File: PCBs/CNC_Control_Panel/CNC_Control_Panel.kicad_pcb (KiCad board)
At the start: 2 copper layers, 100 x 100 mm, 45 parts, among them J1 Conn_01x07_Male, P1 Conn_02x20_Odd_Even, X0 SW_Push, Y0 SW_Push

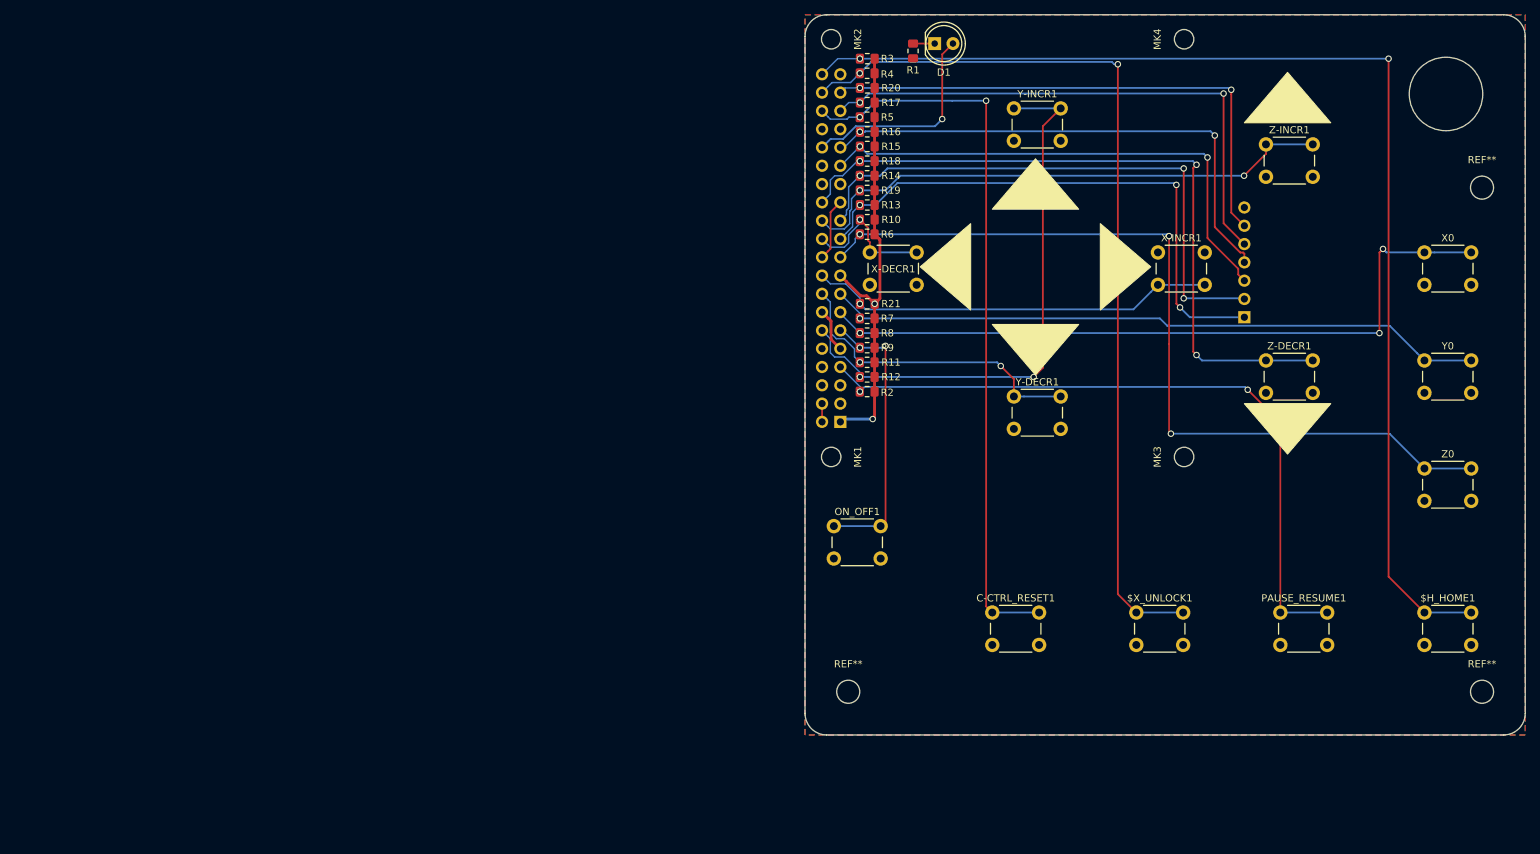
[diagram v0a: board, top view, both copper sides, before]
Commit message: reduced sheet size to A4
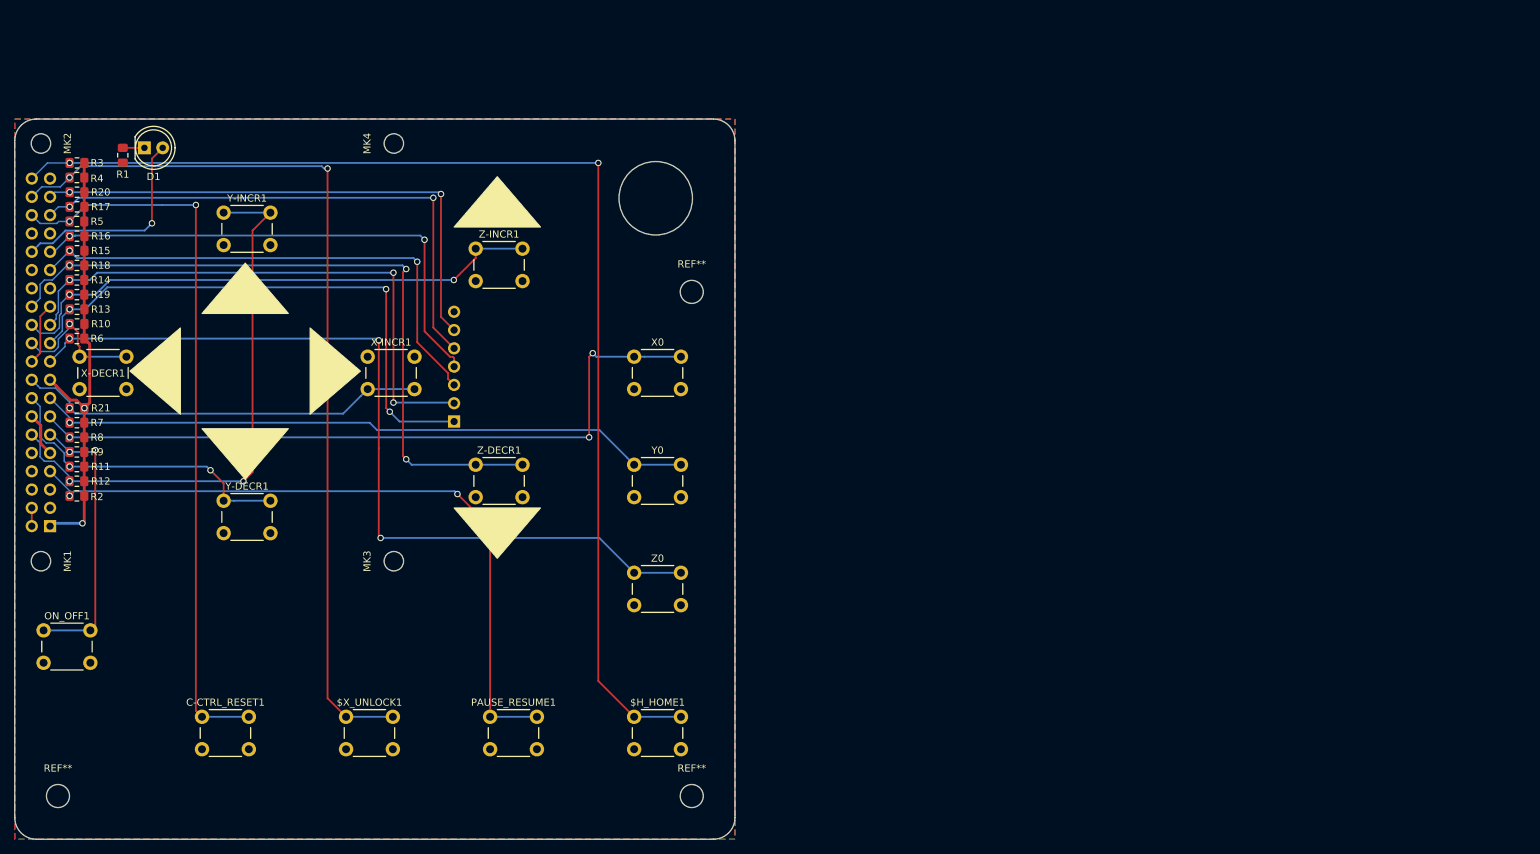
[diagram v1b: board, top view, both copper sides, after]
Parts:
- moved C-CTRL_RESET1 110.7 mm to (60.3, 160.5)
- moved D1 110.7 mm to (52.3, 81.5)
- moved ON_OFF1 110.7 mm to (38.3, 148.5)
- moved R1 110.7 mm to (49.3, 82.5)
- moved R10 110.7 mm to (42.9, 105.9)
- moved R11 110.7 mm to (42.9, 125.7)
- moved R12 110.7 mm to (42.9, 127.8)
- moved R13 110.7 mm to (42.9, 103.9)
- moved R14 110.7 mm to (42.9, 99.8)
- moved R15 110.7 mm to (42.9, 95.8)
- moved R16 110.7 mm to (42.9, 93.7)
- moved R17 110.7 mm to (42.9, 89.7)
- moved R19 110.7 mm to (42.9, 101.9)
- moved R2 110.7 mm to (42.9, 129.8)
- moved R20 110.7 mm to (42.9, 87.6)
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
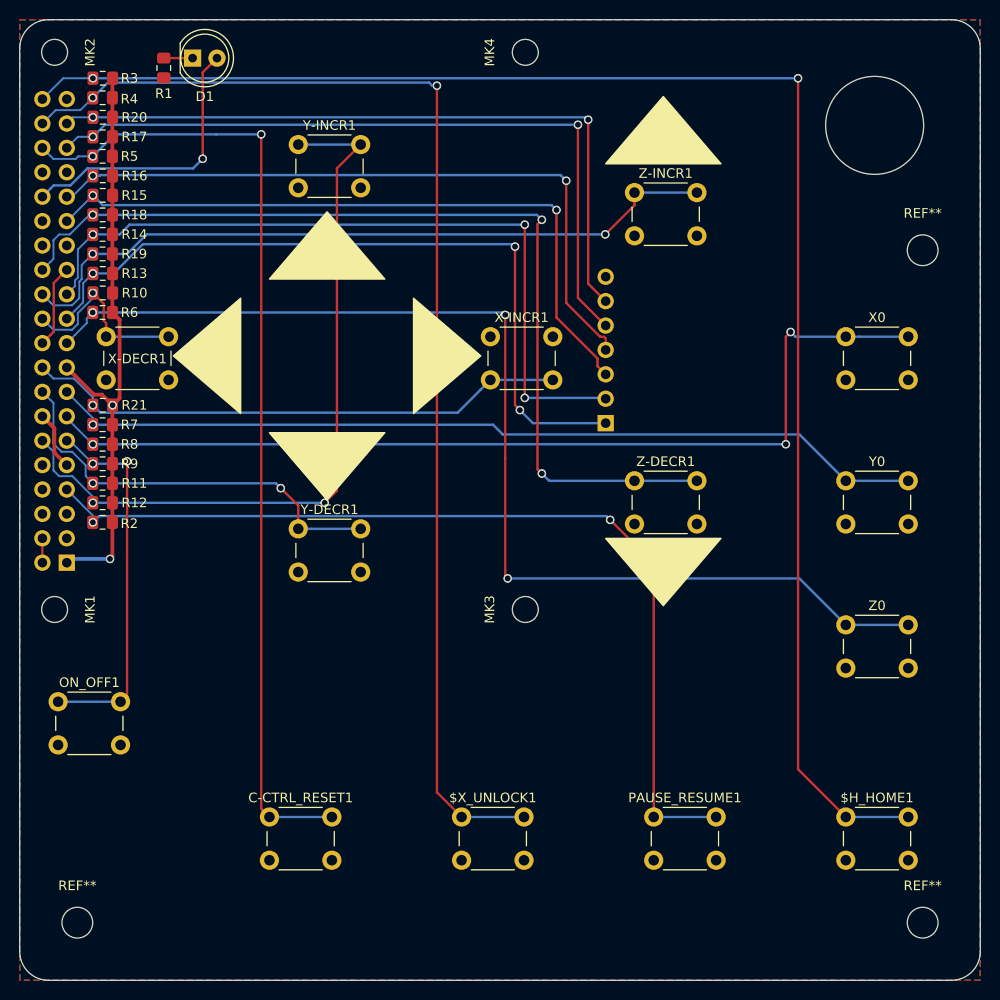
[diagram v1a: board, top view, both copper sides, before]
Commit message: updated layout to the new changes
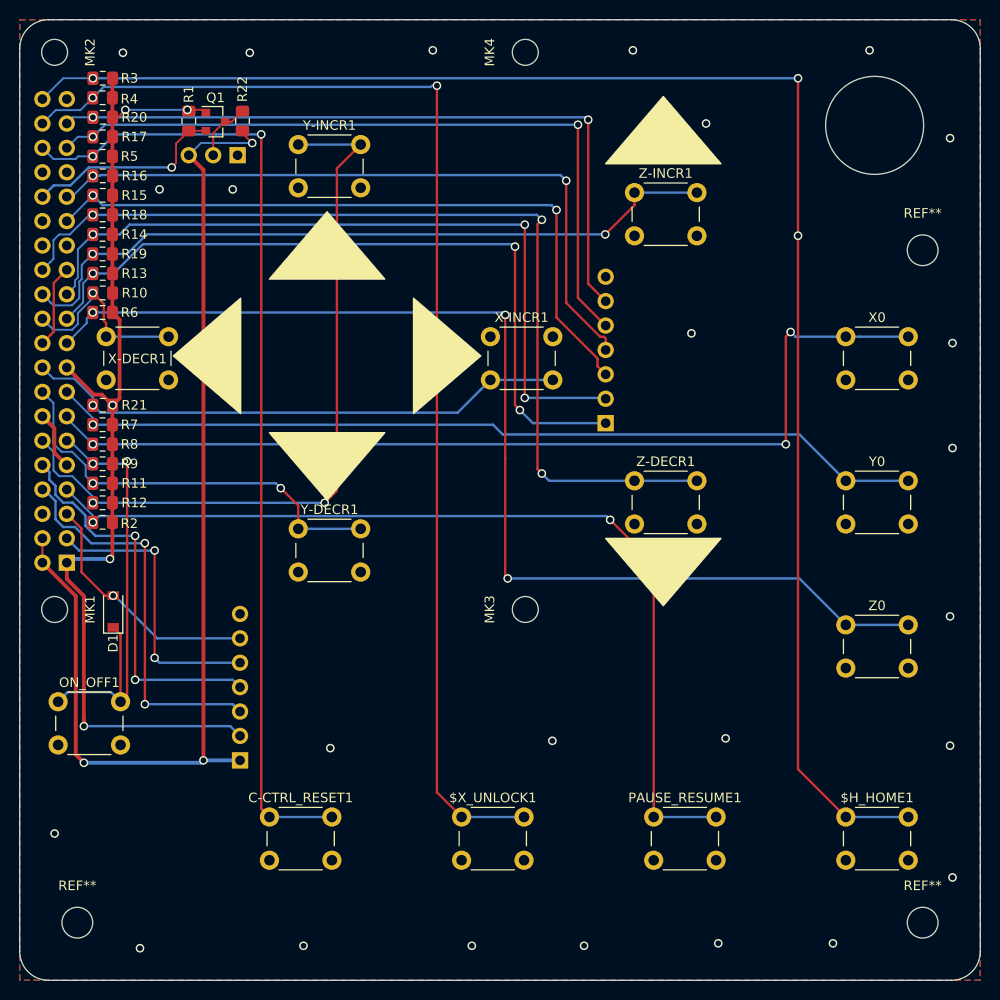
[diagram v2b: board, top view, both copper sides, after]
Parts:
- added J2: Conn_01x03_Male, Connector_PinHeader_2.54mm:PinHeader_1x03_P2.54mm_Horizontal, B.Cu at (57.0, 91.6)
- added J3: Conn_01x07_Male, Connector_PinHeader_2.54mm:PinHeader_1x07_P2.54mm_Horizontal, B.Cu at (57.2, 154.6)
- added Q1: BSS138, Package_TO_SOT_SMD:SOT-23, F.Cu at (54.7, 88.1)
- added R22: 10k, Resistor_SMD:R_0805_2012Metric_Pad1.15x1.40mm_HandSolder, F.Cu at (57.5, 88.0)
- D1: value LED -> 1N4148W; footprint LED_THT:LED_D5.0mm -> Diode_SMD:D_SOD-123
- R1: value 470 -> 10k
- moved D1 58.2 mm to (44.0, 139.1), turned to 90 degrees
- moved R1 6.10 mm to (51.9, 88.0)
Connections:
- D1 pad 1: Net-(D1-Pad1) -> /GPIO17(GEN0)
- D1 pad 2: /GPIO12(PWM0) -> /GPIO3(SCL1)
- R1 pad 1: Net-(D1-Pad1) -> +3V3
- R1 pad 2: GND -> /GPIO12(PWM0)
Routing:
- net +5V: track 2.54 -> 114.0 mm, vias 0 -> 3
- net +3V3: track 61.8 -> 106.4 mm, vias 2 -> 5
- net /GPIO14(TXD0): track 0.00 -> 41.1 mm, vias 0 -> 2
- net /GPIO15(RXD0): track 0.00 -> 40.6 mm, vias 0 -> 2
- net /GPIO2(SDA1): track 0.00 -> 30.0 mm, vias 0 -> 2
- net /GPIO3(SCL1): track 0.00 -> 26.1 mm, vias 0 -> 1
- net /GPIO17(GEN0): track 39.2 -> 48.1 mm
- net /GPIO12(PWM0): track 29.5 -> 21.0 mm
- net Net-(J2-Pad2): track 0.00 -> 6.30 mm
- net Net-(D1-Pad1): track 3.00 -> 0.00 mm
- net GND: vias 0 -> 25
- net /GPIO21(SPI1_SCK): vias 2 -> 3

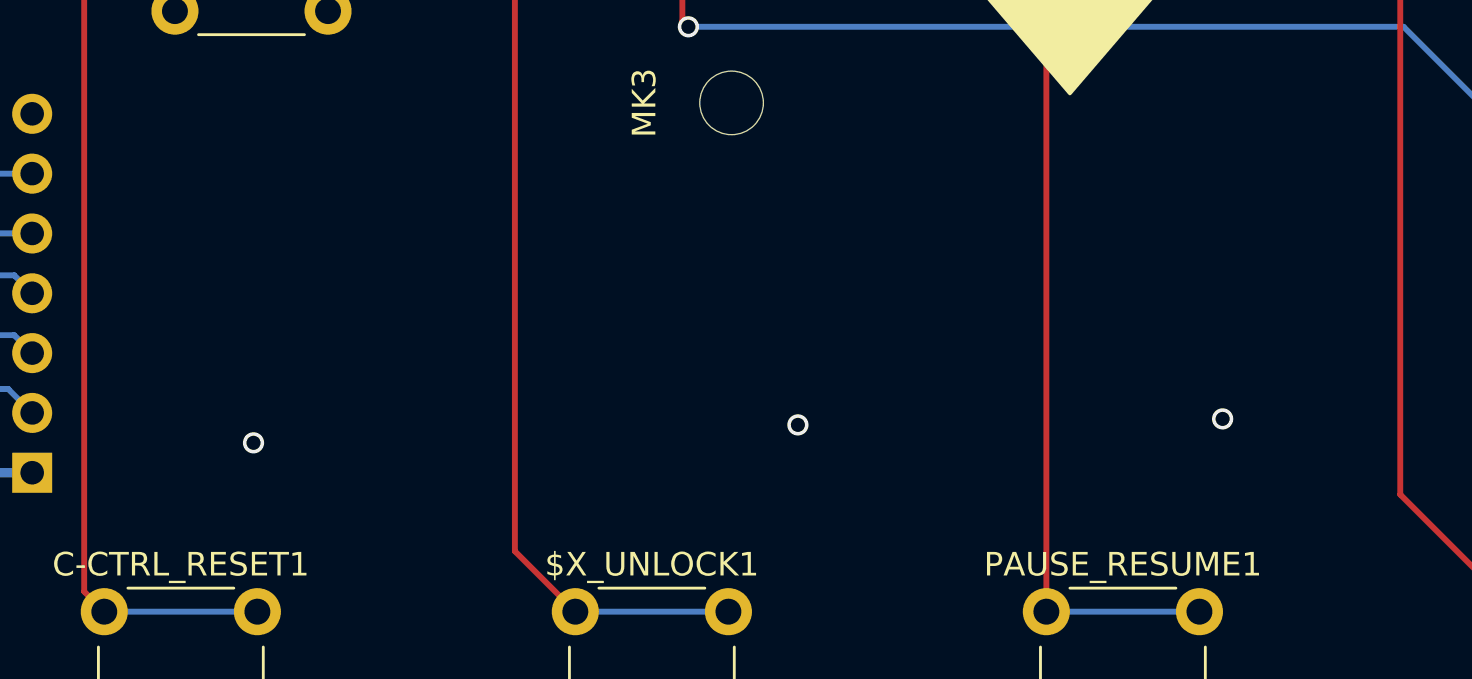
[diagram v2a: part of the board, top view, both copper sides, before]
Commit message: added better silkscreen labeling & logo
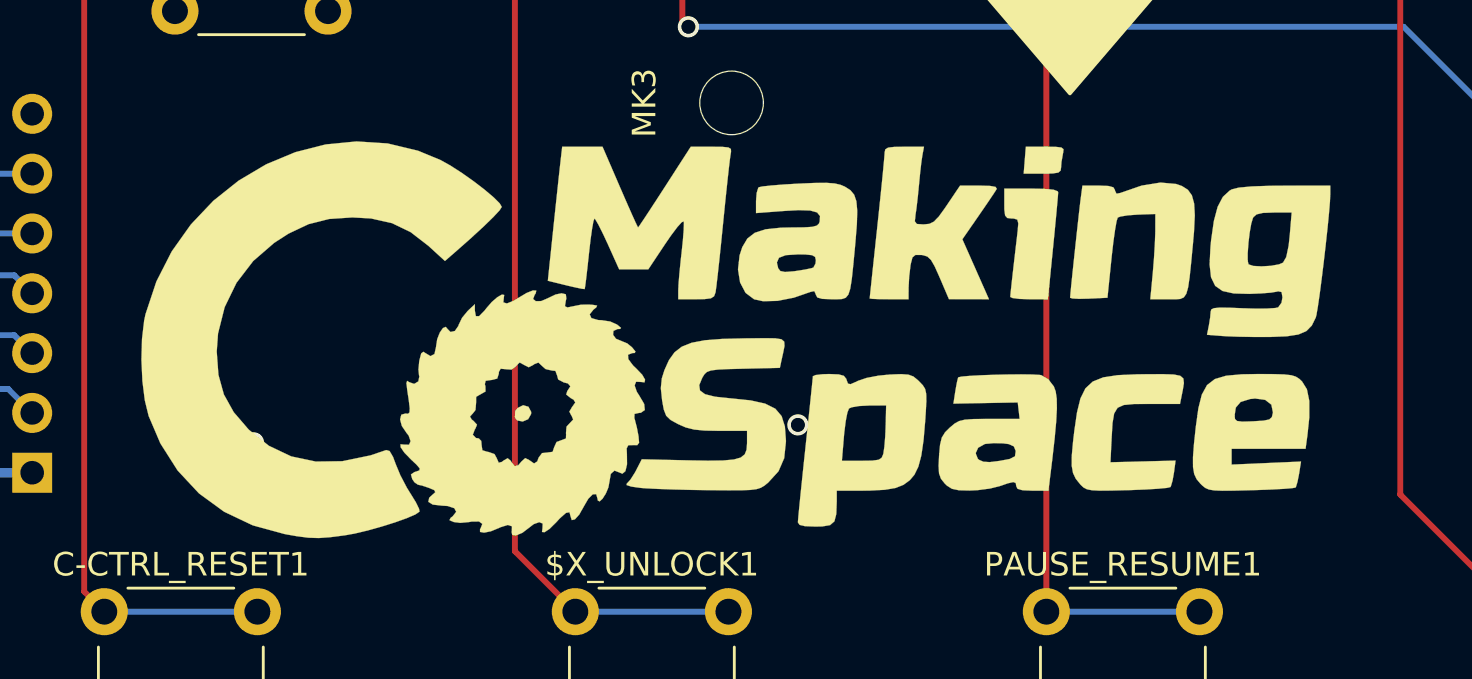
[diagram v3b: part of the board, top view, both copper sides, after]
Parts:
- added G***: LOGO, Graphics:CoMakingSpace_Logo, F.Cu at (87.2, 149.0)

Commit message: updated 3D renders
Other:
- board text added: "1"
- board text added: "2"
- board text added: "3"
- board text added: "3V3"
- board text added: "4"
- board text added: "5"
- board text added: "5V"
- board text added: "6"
- board text added: "GND"
- board text added: "NeoPixel"
- board text added: "RX"
- board text added: "Rotary Switch"
- board text added: "SCL"
- board text added: "SDA"
- board text added: "TX"
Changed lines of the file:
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@@
   (general
     (thickness 1.6)
-    (drawings 33)
+    (drawings 49)
     (tracks 400)
     (zones 0)
@@
     (descr "Through hole angled pin header, 1x07, 2.54mm pitch, 6mm pin length, single row")
     (tags "Through hole angled pin header THT 1x07 2.54mm single row")
-    (fp_text reference J1 (at 4.385 2.27) (layer B.SilkS)
+    (fp_text reference J1 (at 11.214 2.27) (layer B.SilkS)
       (effects (font (size 1 1) (thickness 0.15)) (justify mirror))
     )
@@
     )
   )
+  (gr_text 5V (at 55.94 154.579) (layer B.SilkS)
+    (effects (font (size 1 1) (thickness 0.25)) (justify left mirror))
+  )
+  (gr_text 3V3 (at 55.94 152.039) (layer B.SilkS)
+    (effects (font (size 1 1) (thickness 0.25)) (justify left mirror))
+  )
+  (gr_text TX (at 55.94 149.499) (layer B.SilkS)
+    (effects (font (size 1 1) (thickness 0.25)) (justify left mirror))
+  )
+  (gr_text RX (at 55.94 146.959) (layer B.SilkS)
+    (effects (font (size 1 1) (thickness 0.25)) (justify left mirror))
+  )
+  (gr_text SDA (at 55.94 144.419) (layer B.SilkS)
+    (effects (font (size 1 1) (thickness 0.25)) (justify left mirror))
+  )
+  (gr_text SCL (at 55.94 141.879) (layer B.SilkS)
+    (effects (font (size 1 1) (thickness 0.25)) (justify left mirror))
+  )
+  (gr_text GND (at 55.94 139.339) (layer B.SilkS)
+    (effects (font (size 1 1) (thickness 0.25)) (justify left mirror))
+  )
+  (gr_text NeoPixel (at 57.718 93.873) (layer B.SilkS)
+    (effects (font (size 1 1) (thickness 0.25)) (justify left mirror))
+  )
+  (gr_text 1 (at 94.002 119.478) (layer B.SilkS)
+    (effects (font (size 1 1) (thickness 0.25)) (justify left mirror))
+  )
+  (gr_text 2 (at 94.04 116.987) (layer B.SilkS)
+    (effects (font (size 1 1) (thickness 0.25)) (justify left mirror))
+  )
+  (gr_text 3 (at 94.04 114.447) (layer B.SilkS)
+    (effects (font (size 1 1) (thickness 0.25)) (justify left mirror))
+  )
+  (gr_text 4 (at 94.04 111.907) (layer B.SilkS)
+    (effects (font (size 1 1) (thickness 0.25)) (justify left mirror))
+  )
+  (gr_text 5 (at 94.04 109.367) (layer B.SilkS)
+    (effects (font (size 1 1) (thickness 0.25)) (justify left mirror))
+  )
+  (gr_text 6 (at 94.04 106.827) (layer B.SilkS)
+    (effects (font (size 1 1) (thickness 0.25)) (justify left mirror))
+  )
+  (gr_text GND (at 94.04 104.287) (layer B.SilkS)
+    (effects (font (size 1 1) (thickness 0.25)) (justify left mirror))
+  )
+  (gr_text "Rotary Switch" (at 99.374 121.813) (layer B.SilkS)
+    (effects (font (size 1 1) (thickness 0.25)) (justify mirror))
+  )
   (target plus (at 36.558 85.86) (size 5) (width 0.1) (layer Edge.Cuts))
